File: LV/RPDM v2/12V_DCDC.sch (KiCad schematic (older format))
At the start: 9 parts, among them U1 i7A24045A033V-001-R

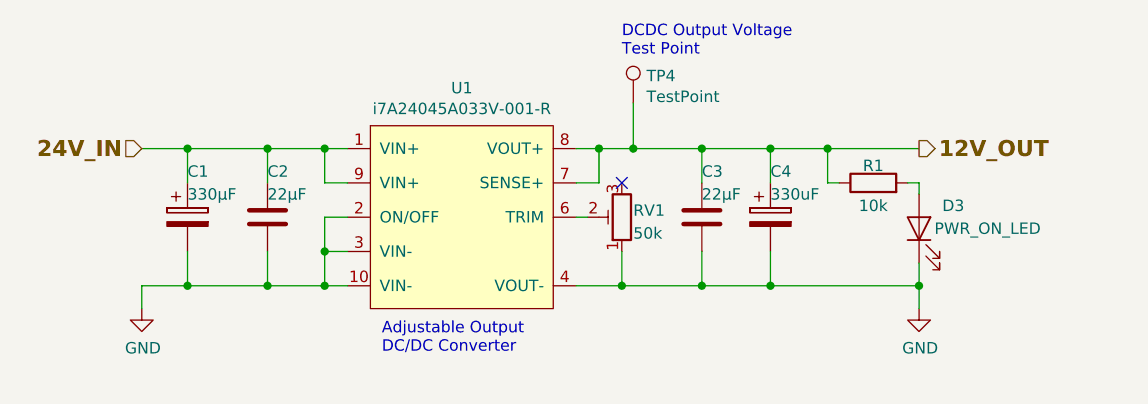
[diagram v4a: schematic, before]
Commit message: rpdm, libraries cleanup
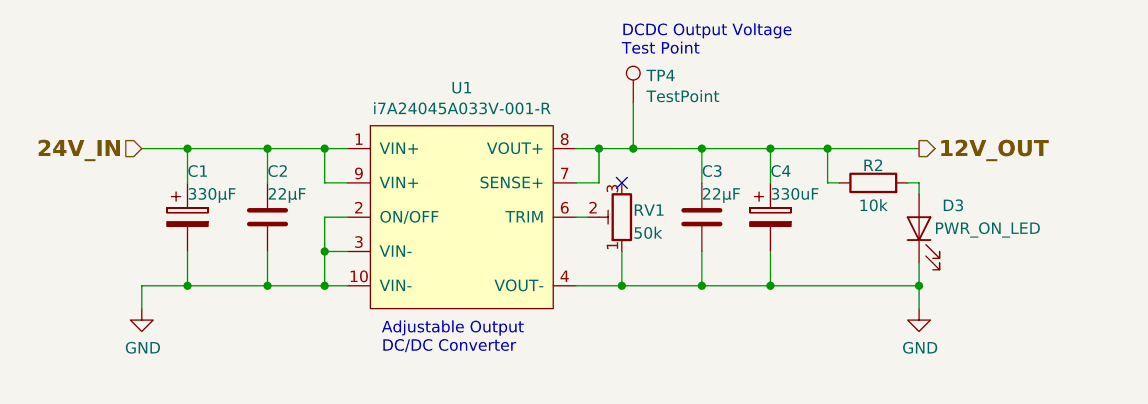
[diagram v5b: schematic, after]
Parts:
- renumbered R1 to R2
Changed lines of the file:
@@
 P 7400 3650
 AR Path="/5E546572/60E34B0B" Ref="R?"  Part="1"
-AR Path="/5E545B2D/60E34B0B" Ref="R1"  Part="1"
+AR Path="/5E545B2D/60E34B0B" Ref="R2"  Part="1"
 AR Path="/5E5461C2/60E34B0B" Ref="R?"  Part="1"
-F 0 "R1" V 7475 3650 50  0000 C CNN
+F 0 "R2" V 7475 3650 50  0000 C CNN
 F 1 "10k" V 7300 3650 50  0000 C CNN
 F 2 "Resistor_SMD:R_0805_2012Metric_Pad1.15x1.40mm_HandSolder" V 7330 3650 50  0001 C CNN

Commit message: RPDM
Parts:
- added R37: 470, Resistor_SMD:R_0805_2012Metric_Pad1.15x1.40mm_HandSolder, symbol Device:R
- C8: renamed from C2; footprint Capacitor_extra:C_Murata_KCM55 -> UOWM_Capacitors:C_Murata_KCM55
- C9: renamed from C3; footprint Capacitor_extra:C_Murata_KCM55 -> UOWM_Capacitors:C_Murata_KCM55
- RV2: renamed from RV1; value 50k -> 1k; footprint (none) -> UOWM_Potentiometers:TRIM_3214W
- U5: renamed from U1; footprint DCDC:i7A24045A033V -> UOWM_DCDCs:i7A24045A033V
- renumbered C4 to C10, C1 to C7, D3 to D29, R2 to R38
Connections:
- net at RV2.2: now also R37.2; no longer U5.6 (TRIM)
- new net: R37.1, U5.6 (TRIM)
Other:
- moved on the sheet: C10, C9, D29, R38, RV2, TP4
